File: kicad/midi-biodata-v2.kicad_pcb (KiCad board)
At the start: 2 copper layers, 63.5 x 45.7 mm, 34 parts, among them J1 DIN-5_180degree, J2 PJ-320B, J3 Conn_01x14_Pin, J5 PJ-320B, J6 PJ-320B, U1 SN74LVC1G07DBVR, U3 LMC555xM

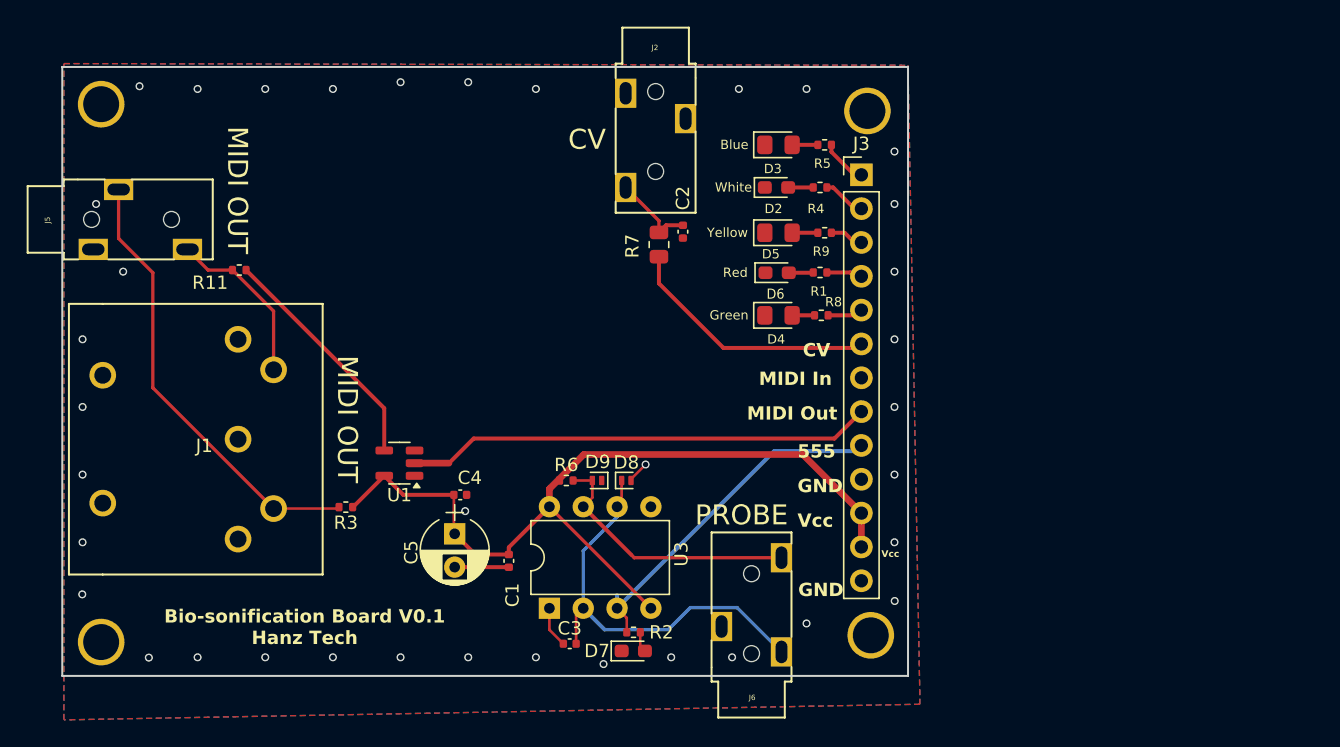
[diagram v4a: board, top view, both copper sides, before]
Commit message: updated board with esp32 s3 mini integration
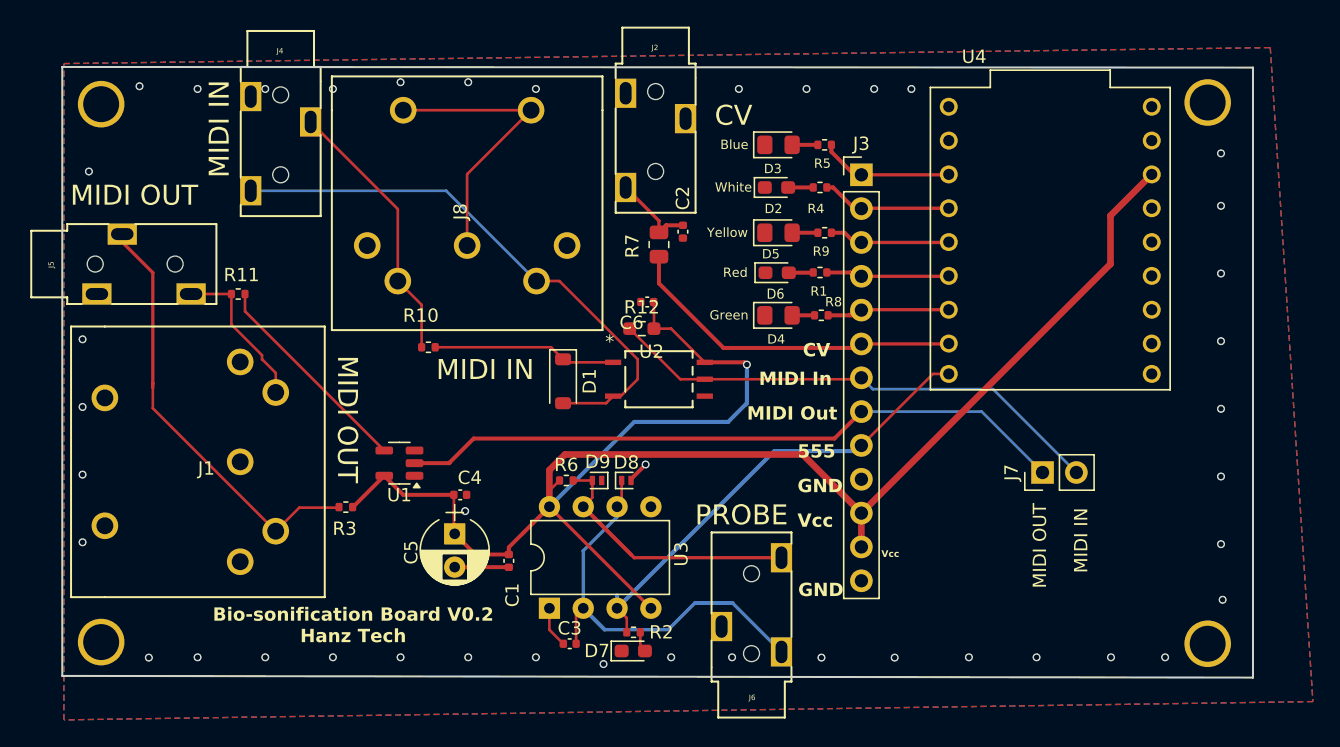
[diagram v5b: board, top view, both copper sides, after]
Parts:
- added C6: 0.1uF, Capacitor_SMD:C_0402_1005Metric, F.Cu at (43.9, -28.2)
- added D1: 1N4148W, Diode_SMD:D_SOD-123, F.Cu at (37.6, -22.2)
- added J4: PJ-320B, poma:3.5mm_stereo_jack_PJ320B_THRU, F.Cu at (16.4, -43.8)
- added J7: Conn_01x02_Socket, Connector_PinHeader_2.54mm:PinHeader_1x02_P2.54mm_Vertical, F.Cu at (73.6, -15.4)
- added J8: DIN-5_180degree, midi-jack:DIN-5-MIDI-JACK, F.Cu at (30.4, -35.0)
- added R10: 220, Resistor_SMD:R_0402_1005Metric, F.Cu at (27.5, -24.8)
- added R12: 470, Resistor_SMD:R_0603_1608Metric_Pad0.98x0.95mm_HandSolder, F.Cu at (43.5, -26.2)
- added U2: TLP2362TPR_E, poma:tlp2362, F.Cu at (44.8, -22.4)
- added U4: ESP32-S3_SUPERMINI_TH, esp32s3mini:MODULE_ESP32-C3_SUPERMINI_TH, F.Cu at (74.2, -33.0)
- moved ? 25.6 mm to (86.0, -43.2)
- moved ? 25.3 mm to (86.0, -2.54)
- moved J5 3.36 mm to (2.47, -31.1)
- moved R11 1.80 mm to (13.2, -28.8)
- moved J1 1.71 mm to (10.8, -16.2)
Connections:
- net VCC renamed +3V3
- J3 pad 7: POT_1 -> MIDI_IN
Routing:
- net +3V3: track 68.0 -> 134.4 mm, vias 0 -> 1
- net Net-(D1-A): track 0.00 -> 42.1 mm
- net MIDI_IN: track 0.00 -> 38.5 mm
- net unconnected-(J8-Pad2): track 0.00 -> 21.7 mm
- net Net-(J4-Pad3): track 0.00 -> 20.4 mm
- net MIDI_OUT: track 35.6 -> 51.1 mm
- net Net-(D1-K): track 0.00 -> 13.8 mm
- net 555: track 26.3 -> 35.1 mm
- net LED_GREEN: track 2.56 -> 10.2 mm
- net LED_YELLOW: track 2.77 -> 9.34 mm
- net LED_RED: track 2.93 -> 9.51 mm
- net LED_WHITE: track 3.47 -> 10.0 mm
- net LED_BLUE: track 3.71 -> 10.3 mm
- net CV: track 19.3 -> 25.9 mm
- net /MIDI_1_BUF_OUT: track 17.8 -> 16.1 mm
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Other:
- board size 63.5 x 45.7 mm -> 89.4 x 45.8 mm
- board text added: "Bio-sonification Board V0.2 Hanz Tech"
- board text added: "MIDI IN"
- board text removed: "Bio-sonification Board V0.1 Hanz Tech"

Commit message: fixed esp32s3 board
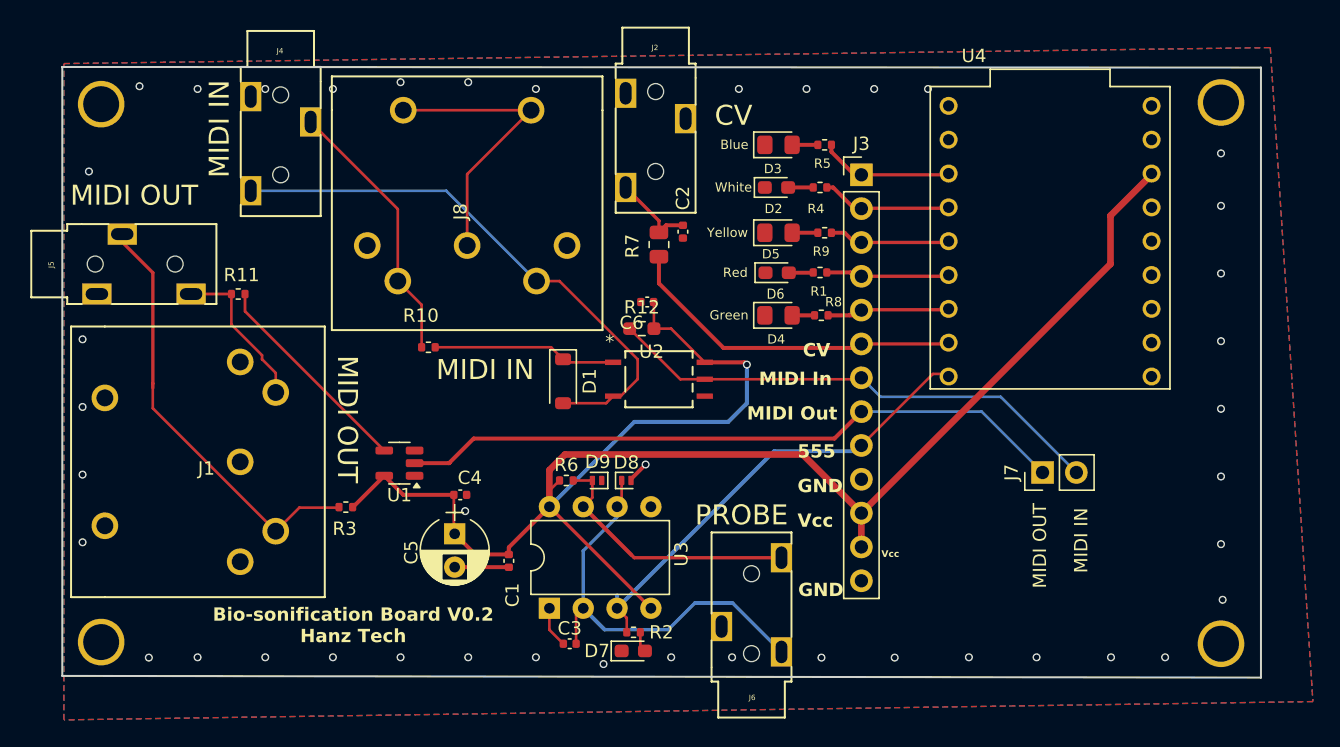
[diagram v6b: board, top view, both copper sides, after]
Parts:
- moved U4 10.9 mm to (66.5, -25.1)
- moved ? 1.00 mm to (87.0, -2.54)
- moved ? 1.00 mm to (87.0, -43.2)
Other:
- board size 89.4 x 45.8 mm -> 90 x 45.8 mm

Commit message: send v0.2 to production
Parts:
- R10: value 220 -> 220R
- R12: footprint Resistor_SMD:R_0603_1608Metric_Pad0.98x0.95mm_HandSolder -> Resistor_SMD:R_0805_2012Metric
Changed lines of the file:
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@@
 			)
 		)
-		(property "Value" "220"
+		(property "Value" "220R"
 			(at 0 1.17 0)
 			(layer "F.Fab")
@@
 		)
 	)
-	(footprint "Resistor_SMD:R_0603_1608Metric_Pad0.98x0.95mm_HandSolder"
+	(footprint "Resistor_SMD:R_0805_2012Metric"
 		(layer "F.Cu")
 		(at 43.5125 -26.2 180)
-		(descr "Resistor SMD 0603 (1608 Metric), square (rectangular) end terminal, IPC_7351 nominal with elongated pad for handsoldering. (Body size source: IPC-SM-782 page 72, https://www.pcb-3d.com/wordpress/wp-content/uploads/ipc-sm-782a_amendment_1_and_2.pdf), generated with kicad-footprint-generator")
-		(tags "resistor handsolder")
+		(descr "Resistor SMD 0805 (2012 Metric), square (rectangular) end terminal, IPC_7351 nominal, (Body size source: IPC-SM-782 page 72, https://www.pcb-3d.com/wordpress/wp-content/uploads/ipc-sm-782a_amendment_1_and_2.pdf), generated with kicad-footprint-generator")
+		(tags "resistor")
 		(property "Reference" "R12"
-			(at 0 1.6 360)
+			(at 0 -1.65 180)
 			(layer "F.SilkS")
 			(effects
@@
 		)
 		(property "Value" "470"
-			(at 0 1.43 360)
+			(at 0 1.65 180)
 			(layer "F.Fab")
 			(effects
@@
 			)
 		)
-		(property "Footprint" "Resistor_SMD:R_0603_1608Metric_Pad0.98x0.95mm_HandSolder"
+		(property "Footprint" "Resistor_SMD:R_0805_2012Metric"
 			(at 0 0 180)
 			(unlocked yes)
@@
 		(attr smd)
 		(fp_line
-			(start -0.254724 0.5225)
-			(end 0.254724 0.5225)
+			(start -0.227064 0.735)
+			(end 0.227064 0.735)
 			(stroke
 				(width 0.12)
@@
 		)
 		(fp_line
-			(start -0.254724 -0.5225)
-			(end 0.254724 -0.5225)
+			(start -0.227064 -0.735)
+			(end 0.227064 -0.735)
 			(stroke
 				(width 0.12)
@@
 		)
 		(fp_line
-			(start 1.65 0.73)
-			(end -1.65 0.73)
+			(start 1.68 0.95)
+			(end -1.68 0.95)
 			(stroke
 				(width 0.05)
@@
 		)
 		(fp_line
-			(start 1.65 -0.73)
-			(end 1.65 0.73)
+			(start 1.68 -0.95)
+			(end 1.68 0.95)
 			(stroke
 				(width 0.05)
@@
 		)
 		(fp_line
-			(start -1.65 0.73)
-			(end -1.65 -0.73)
+			(start -1.68 0.95)
+			(end -1.68 -0.95)
 			(stroke
 				(width 0.05)
@@
 		)
 		(fp_line
-			(start -1.65 -0.73)
-			(end 1.65 -0.73)
+			(start -1.68 -0.95)
+			(end 1.68 -0.95)
 			(stroke
 				(width 0.05)
@@
 		)
 		(fp_line
-			(start 0.8 0.4125)
-			(end -0.8 0.4125)
+			(start 1 0.625)
+			(end -1 0.625)
 			(stroke
 				(width 0.1)
@@
 		)
 		(fp_line
-			(start 0.8 -0.4125)
-			(end 0.8 0.4125)
+			(start 1 -0.625)
+			(end 1 0.625)
 			(stroke
 				(width 0.1)
@@
 		)
 		(fp_line
-			(start -0.8 0.4125)
-			(end -0.8 -0.4125)
+			(start -1 0.625)
+			(end -1 -0.625)
 			(stroke
 				(width 0.1)
@@
 		)
 		(fp_line
-			(start -0.8 -0.4125)
-			(end 0.8 -0.4125)
+			(start -1 -0.625)
+			(end 1 -0.625)
 			(stroke
 				(width 0.1)
@@
 		)
 		(fp_text user "${REFERENCE}"
-			(at 0 0 360)
+			(at 0 0 180)
 			(layer "F.Fab")
 			(effects
 				(font
-					(size 0.4 0.4)
-					(thickness 0.06)
+					(size 0.5 0.5)
+					(thickness 0.08)
 				)
 			)
@@
 		(pad "1" smd roundrect
 			(at -0.9125 0 180)
-			(size 0.975 0.95)
+			(size 1.025 1.4)
 			(layers "F.Cu" "F.Paste" "F.Mask")
-			(roundrect_rratio 0.25)
+			(roundrect_rratio 0.243902)
 			(net 22 "+3V3")
 			(pintype "passive")
@@
 		(pad "2" smd roundrect
 			(at 0.9125 0 180)
-			(size 0.975 0.95)
+			(size 1.025 1.4)
 			(layers "F.Cu" "F.Paste" "F.Mask")
-			(roundrect_rratio 0.25)
+			(roundrect_rratio 0.243902)
 			(net 31 "MIDI_IN")
 			(pintype "passive")
 		)
-		(model "${KICAD8_3DMODEL_DIR}/Resistor_SMD.3dshapes/R_0603_1608Metric.wrl"
+		(model "${KICAD8_3DMODEL_DIR}/Resistor_SMD.3dshapes/R_0805_2012Metric.wrl"
 			(offset
 				(xyz 0 0 0)
@@
 	)
 	(gr_text "Blue"
-		(at 49.4 -39.6 0)
+		(at 56.134 -41.148 0)
 		(layer "F.SilkS")
 		(effects
@@
 	)
 	(gr_text "GND"
-		(at 55.25 -6 0)
+		(at 61.722 -6.604 0)
 		(layer "F.SilkS")
 		(effects
@@
 	)
 	(gr_text "Vcc"
-		(at 61.5 -9 0)
+		(at 61.722 -9.144 0)
 		(layer "F.SilkS")
 		(effects
 			(font
-				(size 0.5 0.5)
-				(thickness 0.125)
+				(size 1 1)
+				(thickness 0.25)
 				(bold yes)
 			)
@@
 	)
 	(gr_text "MIDI OUT"
-		(at 5.4 -36.2 0)
+		(at 5.842 -35.56 0)
 		(layer "F.SilkS")
 		(effects
@@
 	)
 	(gr_text "GND"
-		(at 55.2 -13.8 0)
+		(at 61.722 -14.224 0)
 		(layer "F.SilkS")
 		(effects
@@
 	)
 	(gr_text "PROBE"
-		(at 51 -12.2 0)
+		(at 51.816 -12.2 0)
 		(layer "F.SilkS")
 		(effects
@@
 	)
 	(gr_text "555"
-		(at 55.2 -16.4 0)
+		(at 61.722 -16.764 0)
 		(layer "F.SilkS")
 		(effects
@@
 	)
 	(gr_text "Vcc"
-		(at 55.2 -11.2 0)
+		(at 61.722 -11.684 0)
 		(layer "F.SilkS")
 		(effects
@@
 	)
 	(gr_text "CV"
-		(at 50.4 -42.2 0)
+		(at 49.53 -41.148 0)
 		(layer "F.SilkS")
 		(effects

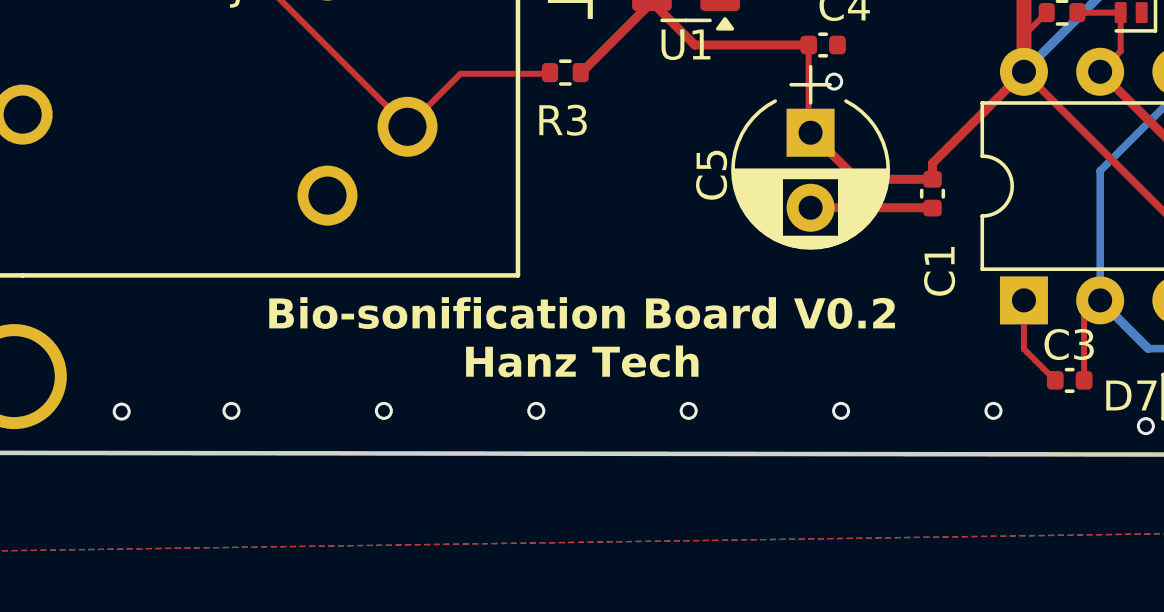
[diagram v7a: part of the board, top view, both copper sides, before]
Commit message: Update MIDI out resistors for 3.3v
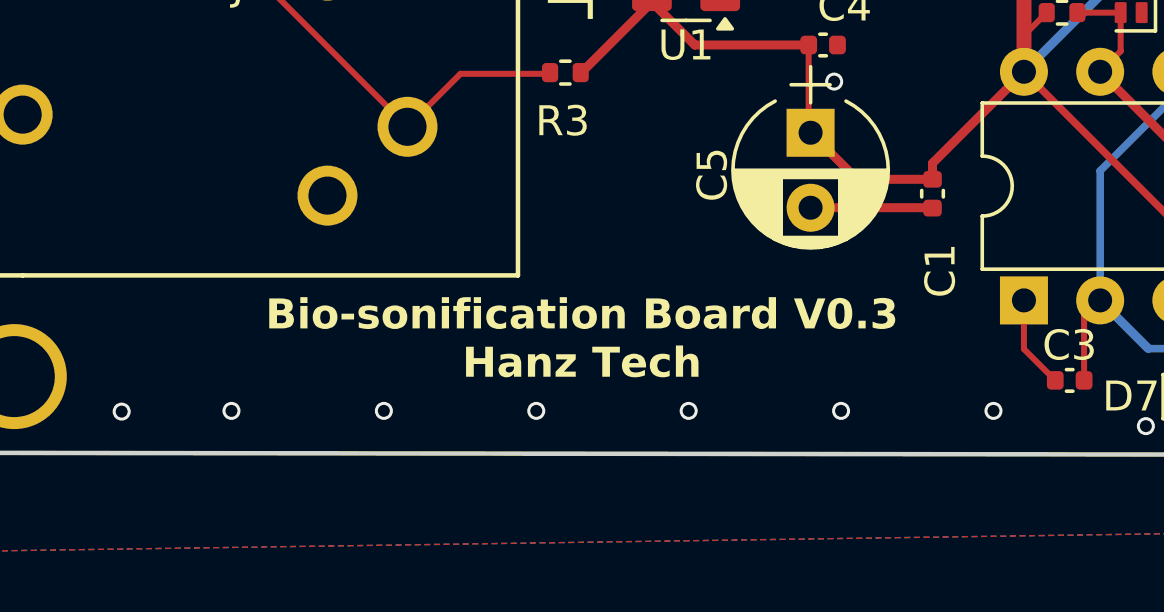
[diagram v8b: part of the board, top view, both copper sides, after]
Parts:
- R11: value 220R -> 10R
- R3: value 220R -> 33R
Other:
- board text added: "Bio-sonification Board V0.3 Hanz Tech"
- board text removed: "Bio-sonification Board V0.2 Hanz Tech"
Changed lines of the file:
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@@
 			)
 		)
-		(property "Value" "220R"
+		(property "Value" "33R"
 			(at 0 1.17 180)
 			(layer "F.Fab")
@@
 			)
 		)
-		(property "LCSC" "C25091"
+		(property "LCSC" "C25105"
 			(at 0 0 180)
 			(unlocked yes)
@@
 			)
 		)
-		(property "Value" "220R"
+		(property "Value" "10R"
 			(at 0 1.17 0)
 			(layer "F.Fab")
@@
 			)
 		)
-		(property "LCSC" "C25091"
+		(property "LCSC" "C25077"
 			(at 0 0 0)
 			(unlocked yes)
@@
 		(tags "capacitor")
 		(property "Reference" "C6"
-			(at 1.175 -1.56 360)
+			(at 1.175 -1.56 0)
 			(layer "F.SilkS")
 			(effects
@@
 		)
 		(property "Value" "0.1uF"
-			(at 0 1.16 360)
+			(at 0 1.16 0)
 			(layer "F.Fab")
 			(effects
@@
 		)
 		(fp_text user "${REFERENCE}"
-			(at 0 0 360)
+			(at 0 0 0)
 			(layer "F.Fab")
 			(effects
@@
 		)
 		(fp_text user "${REFERENCE}"
-			(at 0 1.27 360)
+			(at 0 1.27 0)
 			(layer "F.Fab")
 			(effects
@@
 		)
 	)
-	(gr_text "Bio-sonification Board V0.2\nHanz Tech"
+	(gr_text "Bio-sonification Board V0.3\nHanz Tech"
 		(at 21.844 -2.54 0)
 		(layer "F.SilkS")
